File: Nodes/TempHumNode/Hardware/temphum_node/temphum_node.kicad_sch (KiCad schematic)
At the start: 45 parts, among them IC1 CC1310F128RGZR, IC2 TPD6E004RSER, J1 TC2050-IDC, U1 MCP73123-22SI/MF, U2 SHT35-DIS-B, U3 TPS22860DBVR, U4 TPS63900DSKR, U5 MCP3421A0T-E/CH, Y2 TSX-3225 24.0000MF15X-AC3, Y3 FC-135_32.7680KA-AG0

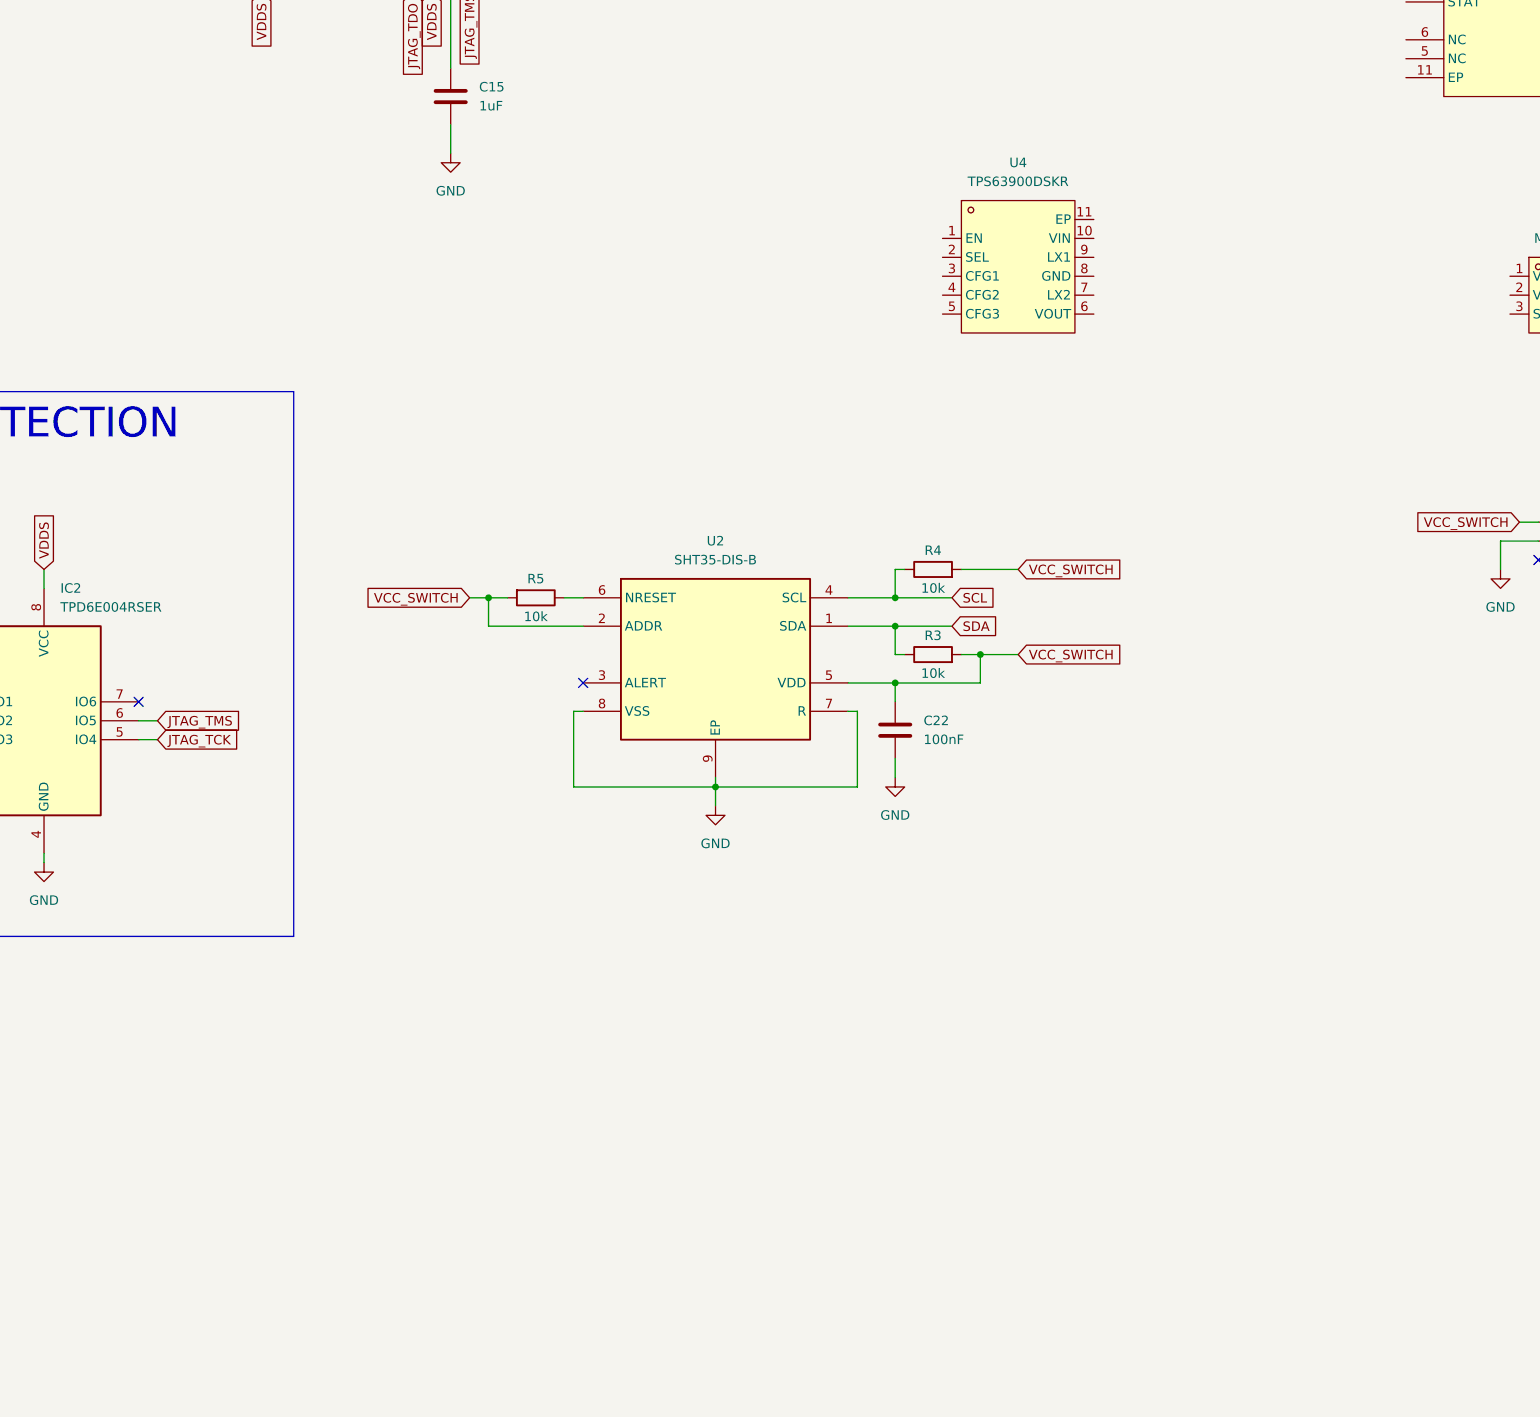
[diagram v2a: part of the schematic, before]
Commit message: hw(temphum-node): add JOIN button (TL3301) + USB-C ESD (USBLC6-2SC6)
JOIN tact switch (LCSC C273519, 6x6 4-pin) wired active-low with
47.5k pull-up + 2.2nF + a TPD6E004 ESD channel. Single-chip USB-C ESD
USBLC6-2SC6 (C7519) for VBUS + CC1/CC2, placed at the connector.

Co-Authored-By: Claude Opus 4.8 (1M context) <noreply@anthropic.com>
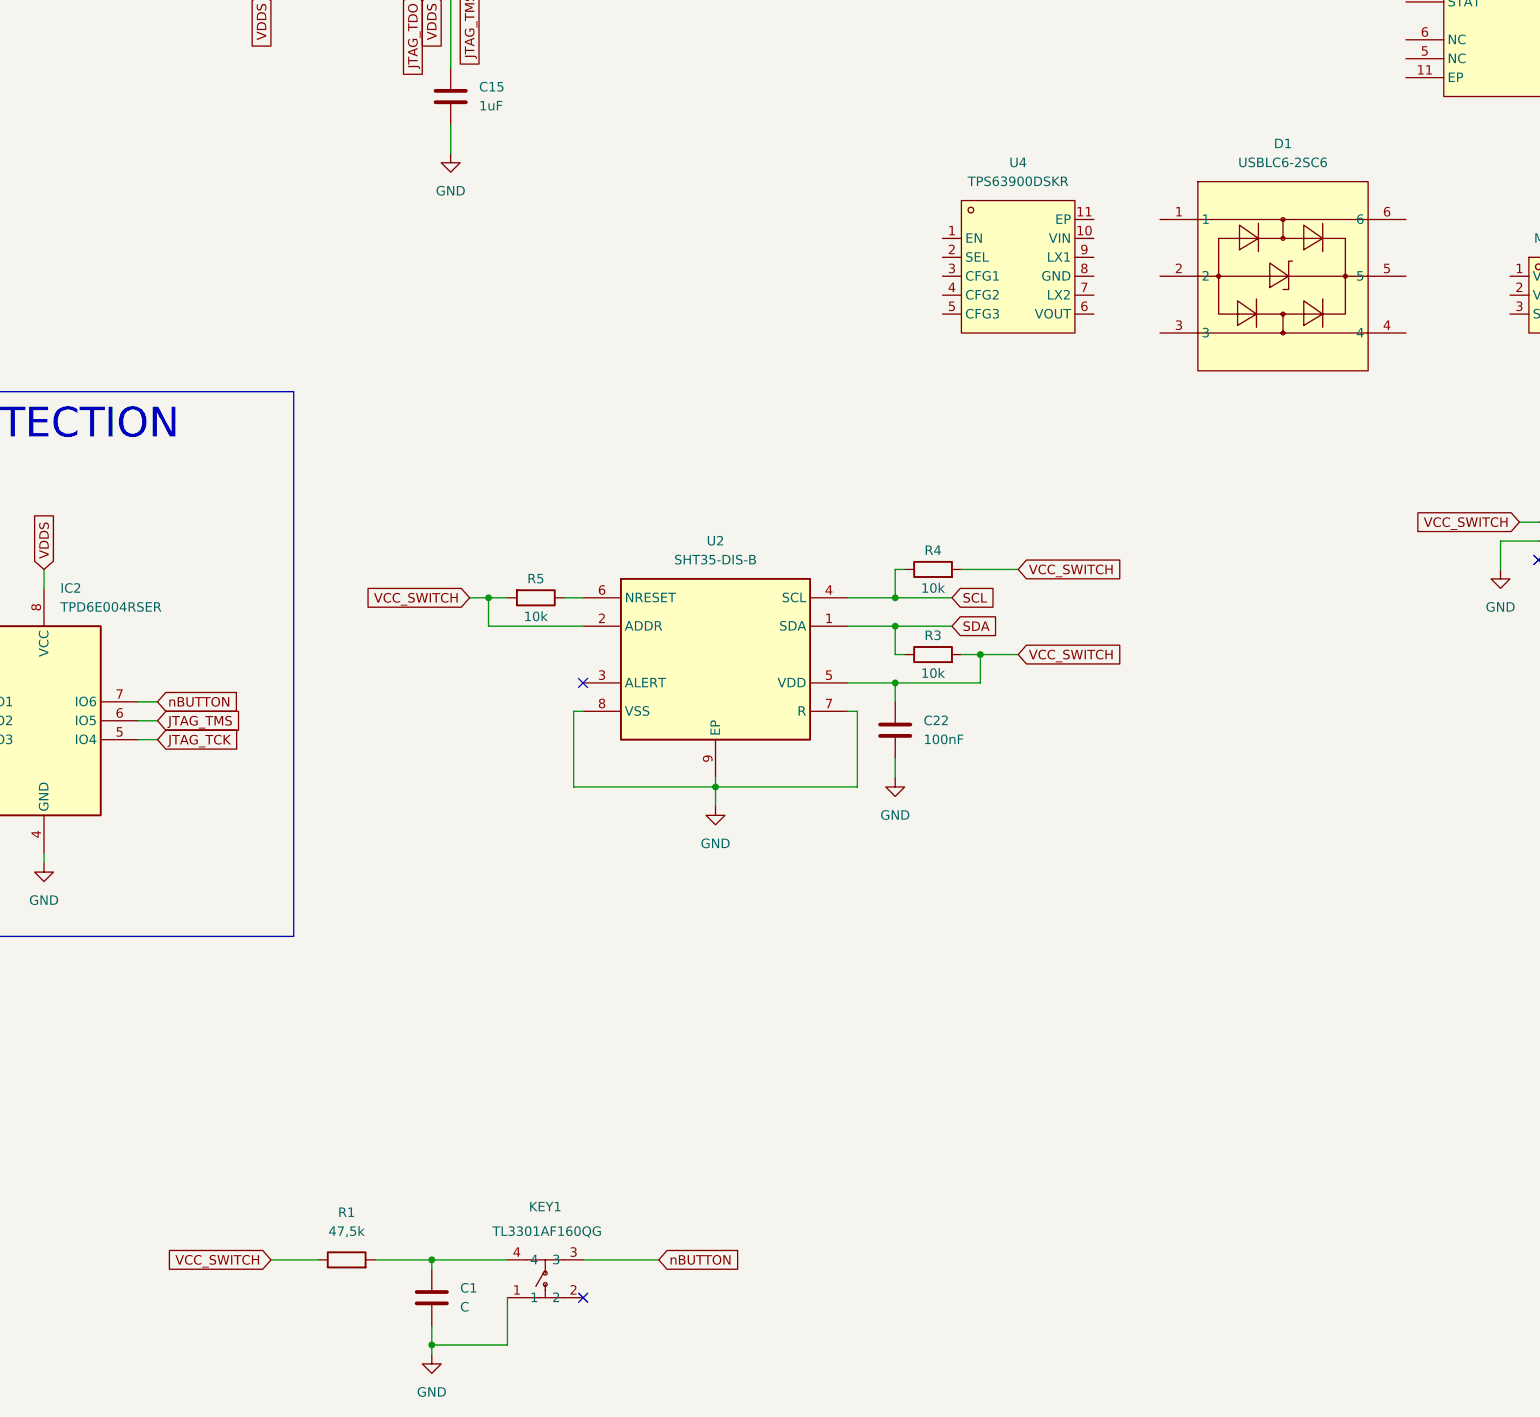
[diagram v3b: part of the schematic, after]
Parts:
- added C1: C, symbol Device:C
- added D1: USBLC6-2SC6, SmartHome:SOT-23-6_L2.9-W1.6-P0.95-LS2.8-BL, symbol SmartHome:USBLC6-2SC6
- added KEY1: TL3301AF160QG, SmartHome:KEY-SMD_4P-L6.0-W6.0-P4.50-LS10.0, symbol SmartHome:TL3301AF160QG
- added R1: 47,5k, symbol Device:R
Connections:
- net GND: now also C1.2, KEY1.1
- net VCC_SWITCH: now also R1.1
- net nBUTTON: now reaches IC2.7 (IO6)
- net nBUTTON: now also KEY1.3
- new net: C1.1, KEY1.4, R1.2

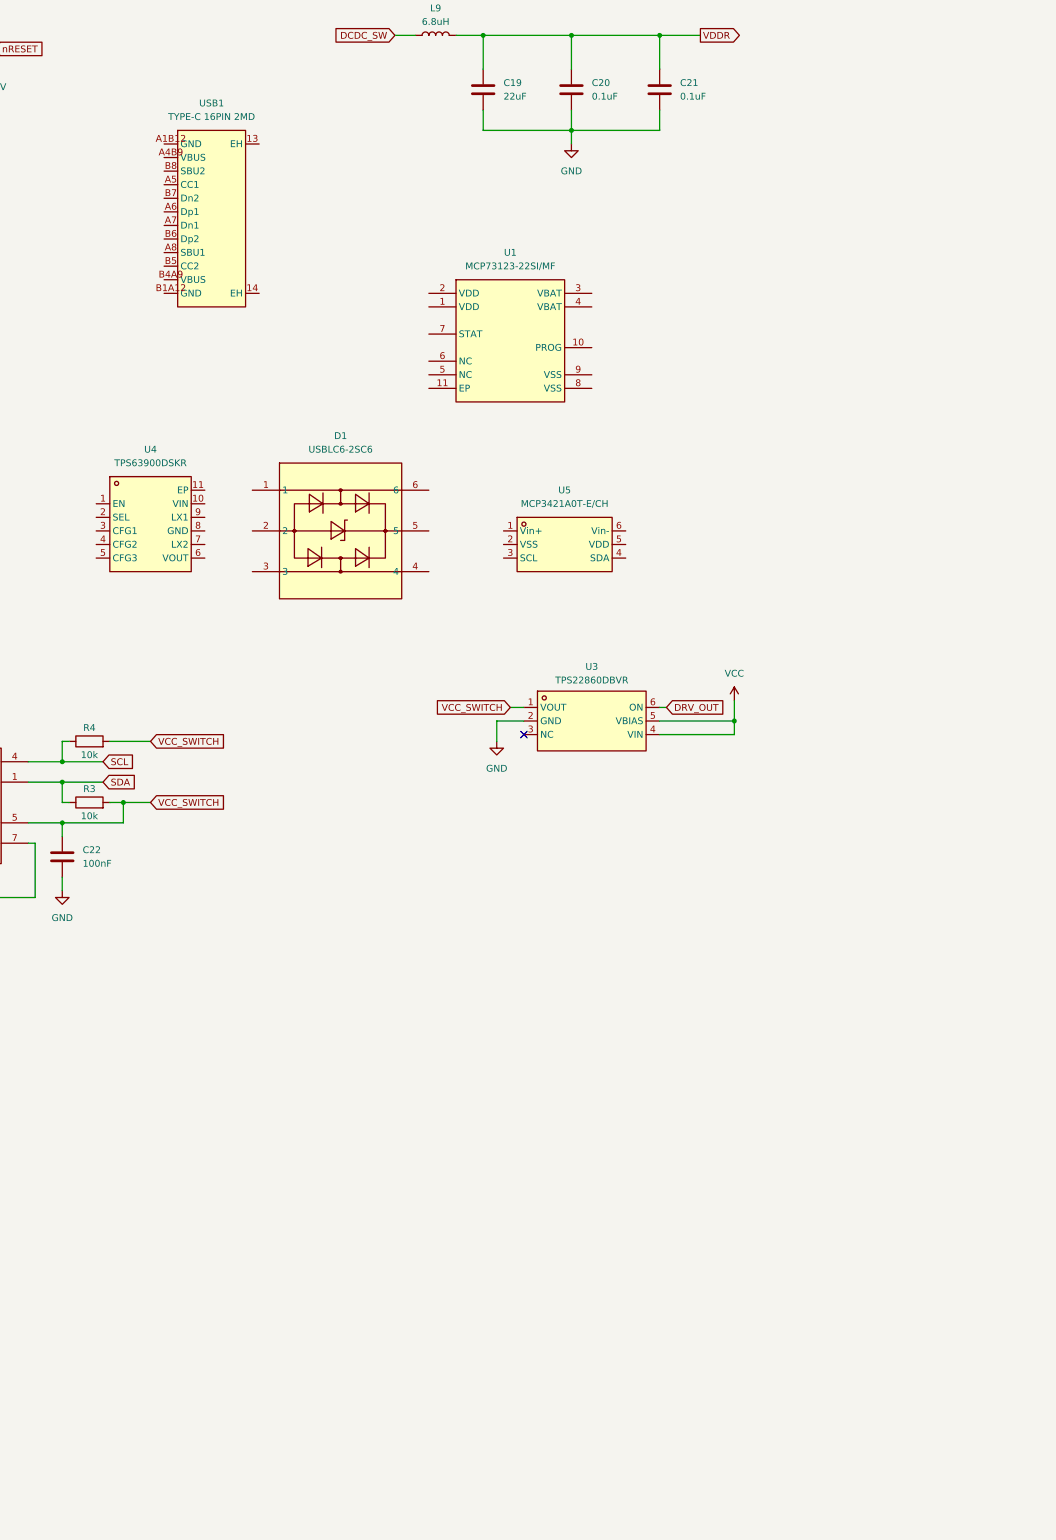
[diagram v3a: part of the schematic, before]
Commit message: hw(temphum-node): wire USB-C front-end + MCP73123 charger
USB-C: 5.1k CC pulldowns, USBLC6-2SC6 ESD (CC1/CC2 on I/O1/I/O2, VBUS
on pin5, GND pin2). Charger: VDD from VBUS + 4.7uF/100nF, PROG 3.0k
(400mA), VBAT->BAT+ +4.7uF, STAT open-drain -> 100k pull-up + red LED
indicator + nCHRGSTAT to CC1310 GPIO, VSS/EP to GND.

Co-Authored-By: Claude Opus 4.8 (1M context) <noreply@anthropic.com>
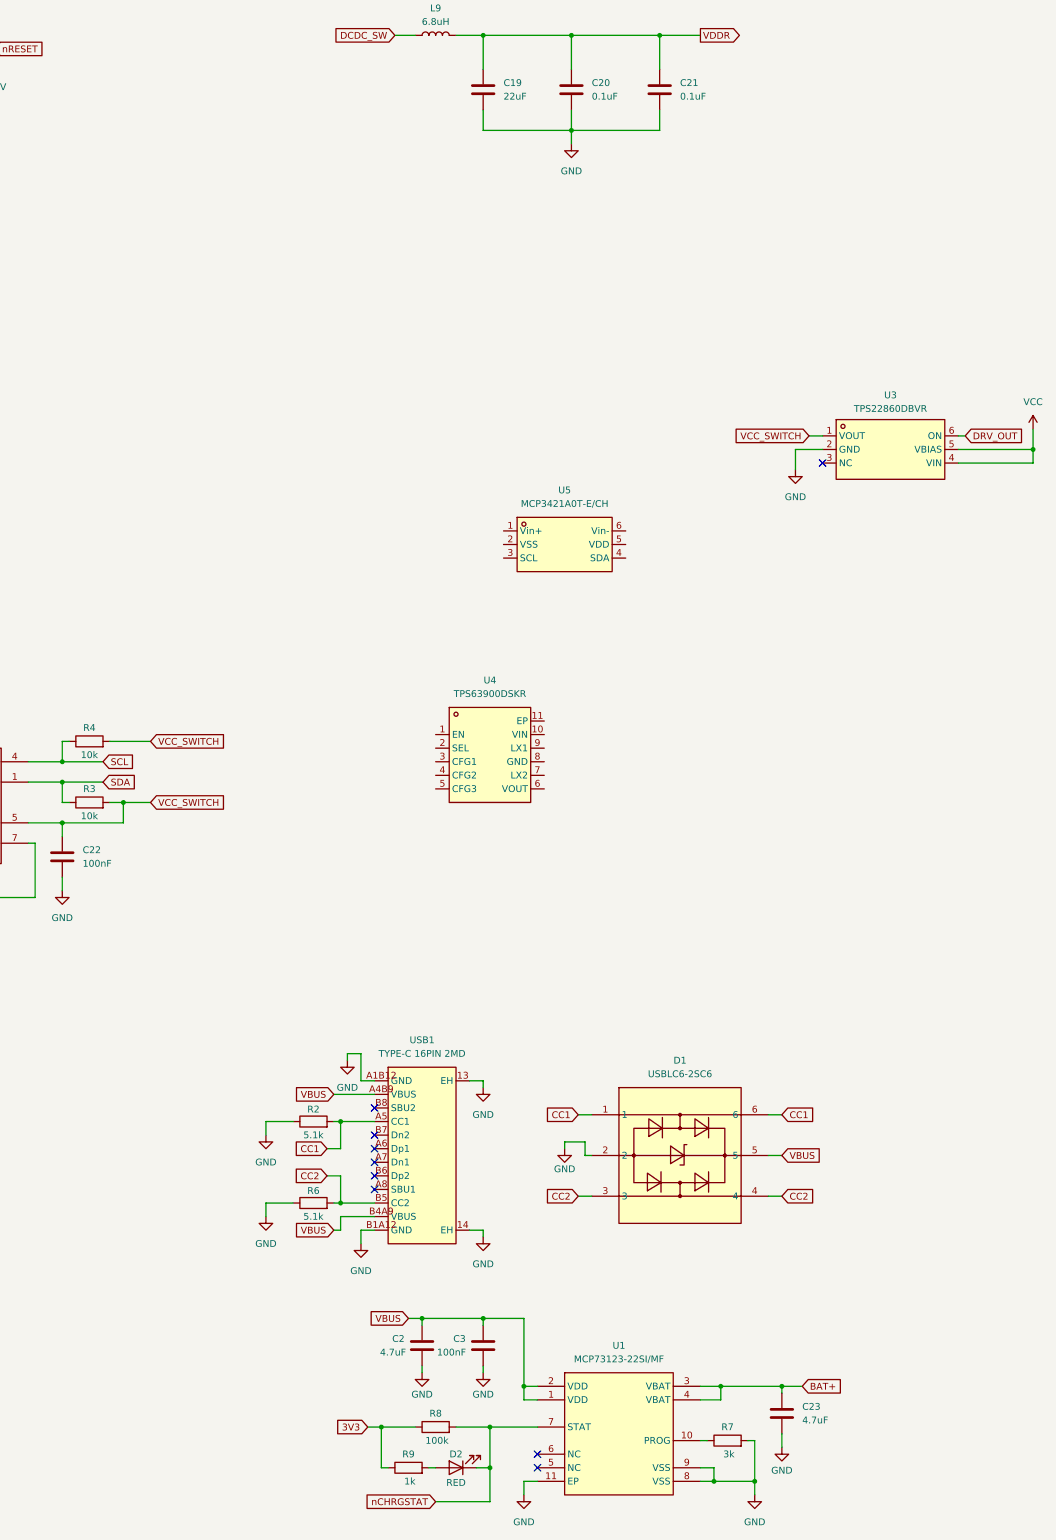
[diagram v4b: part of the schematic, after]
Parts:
- added C2, C23: 4.7uF, symbol Device:C
- added C3: 100nF, symbol Device:C
- added D2: RED, symbol Device:LED
- added R2, R6: 5.1k, symbol Device:R
- added R7: 3k, symbol Device:R
- added R8: 100k, symbol Device:R
- added R9: 1k, symbol Device:R
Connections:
- net 3V3: now also R8.1, R9.1
- net GND: now also D1.2, U1.11 (EP), U1.8 (VSS), U1.9 (VSS), USB1.13 (EH), USB1.14 (EH), USB1.A1B12 (GND), USB1.B1A12 (GND), C2.2, C23.2, C3.2, R2.1, R6.1, R7.2
- net CC1: now reaches D1.1
- net CC1: now also D1.6, USB1.A5 (CC1), R2.2
- net CC2: now reaches D1.3
- net CC2: now also D1.4, USB1.B5 (CC2), R6.2
- net VBUS: now reaches D1.5
- net VBUS: now also U1.1 (VDD), U1.2 (VDD), USB1.A4B9 (VBUS), USB1.B4A9 (VBUS), C2.1, C3.1
- net at U1.10 (PROG): now also R7.1
- net BAT+: now reaches U1.3 (VBAT)
- net BAT+: now also U1.4 (VBAT), C23.1
- net nCHRGSTAT: now reaches U1.7 (STAT)
- net nCHRGSTAT: now also D2.1 (K), R8.2
- new net: D2.2 (A), R9.2
- no-connect marks 28 -> 36
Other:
- moved on the sheet: D1, U1, U3, U4, USB1

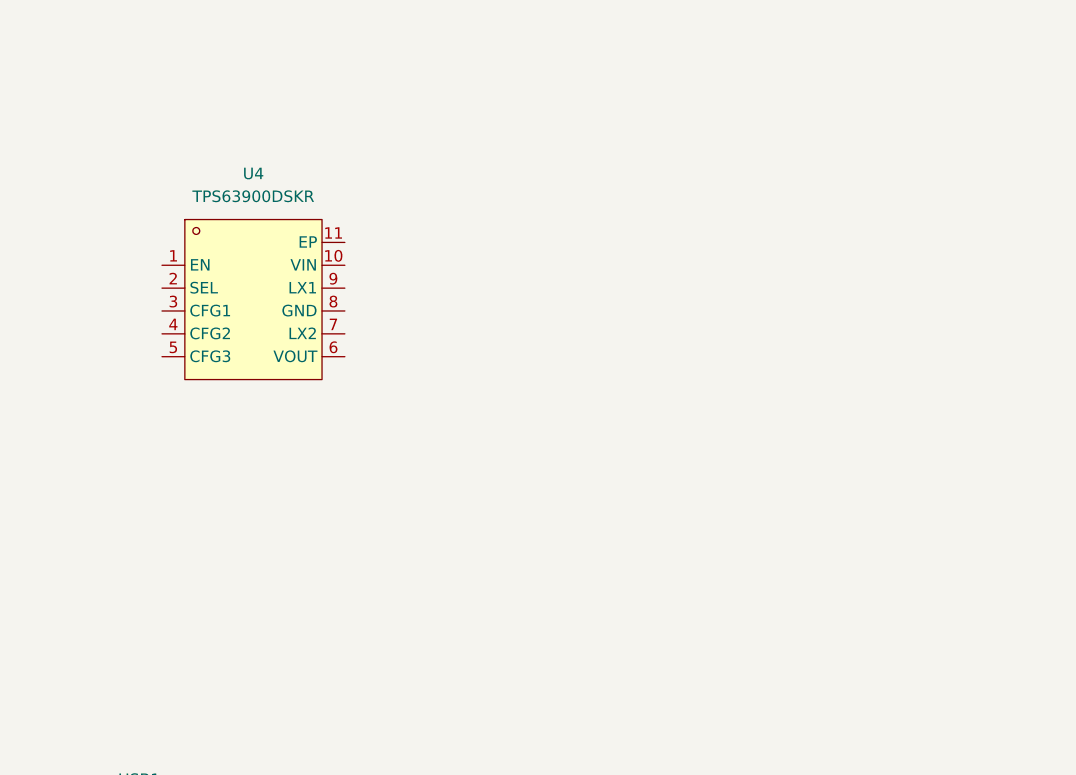
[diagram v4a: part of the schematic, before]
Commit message: hw(temphum-node): wire TPS63900 3.3V buck-boost + add inductor
TPS63900 always-on 3.3V rail: EN/SEL->BAT+ (HIGH, VIH 1.2V << min
LFP), CFG1 36.5k (VOUTH 3.3V), CFG2/CFG3 to GND, Cin 10uF, Cout 22uF,
2.2uH inductor between LX1/LX2. Add Murata DFE252012 2.2uH shielded
inductor (LCSC C237482).

Co-Authored-By: Claude Opus 4.8 (1M context) <noreply@anthropic.com>
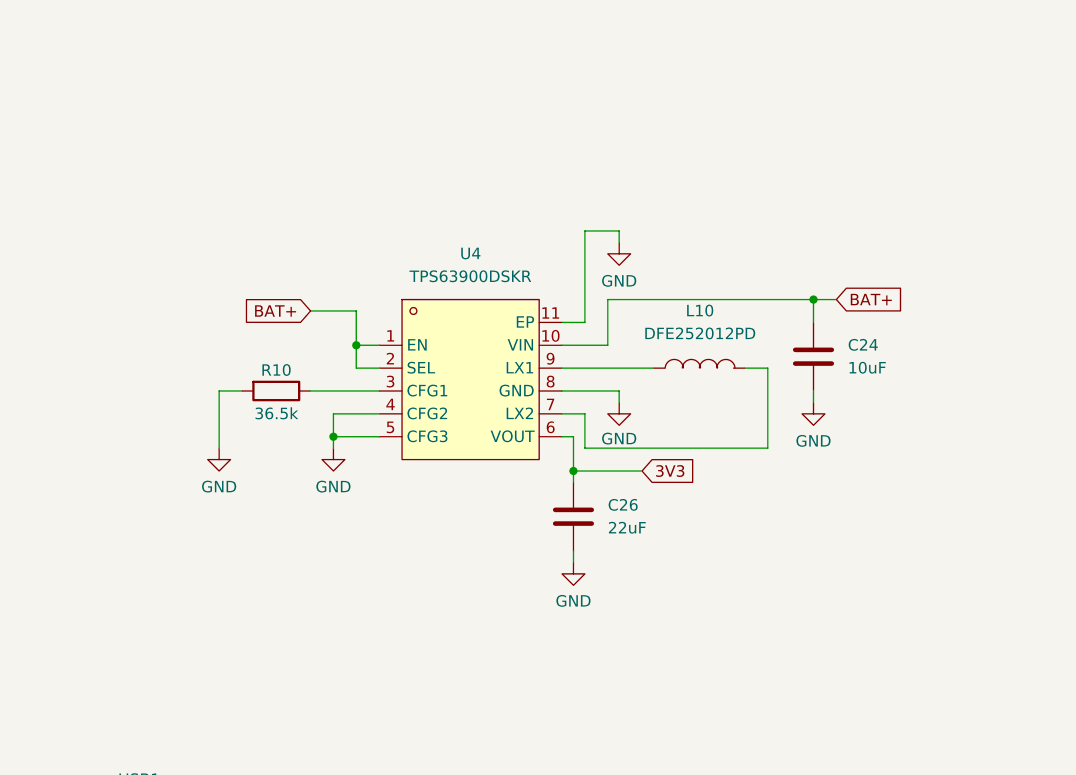
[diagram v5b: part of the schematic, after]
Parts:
- added C24: 10uF, symbol Device:C
- added C26: 22uF, symbol Device:C
- added L10: DFE252012PD, SmartHome:L1008, symbol SmartHome:DFE252012PD-2R2M=P2
- added R10: 36.5k, symbol Device:R
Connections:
- net 3V3: now also U4.6 (VOUT), C26.1
- net BAT+: now also U4.1 (EN), U4.10 (VIN), U4.2 (SEL), C24.1
- net GND: now also U4.11 (EP), U4.4 (CFG2), U4.5 (CFG3), U4.8 (GND), C24.2, C26.2, R10.2
- net at U4.3 (CFG1): now also R10.1
- net at U4.7 (LX2): now also L10.2
- net at U4.9 (LX1): now also L10.1
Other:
- moved on the sheet: U4
